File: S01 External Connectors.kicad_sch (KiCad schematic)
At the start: 43 parts, among them J1 1053101204, J2 1053101114, J3 10144517-043802LF, J4 1053102204, J5 1053091102, J6 1053091102, M1 78614150960, M2 78614150960, M3 78614150960, M4 78614150960, M5 78614150960, M6 78614150960

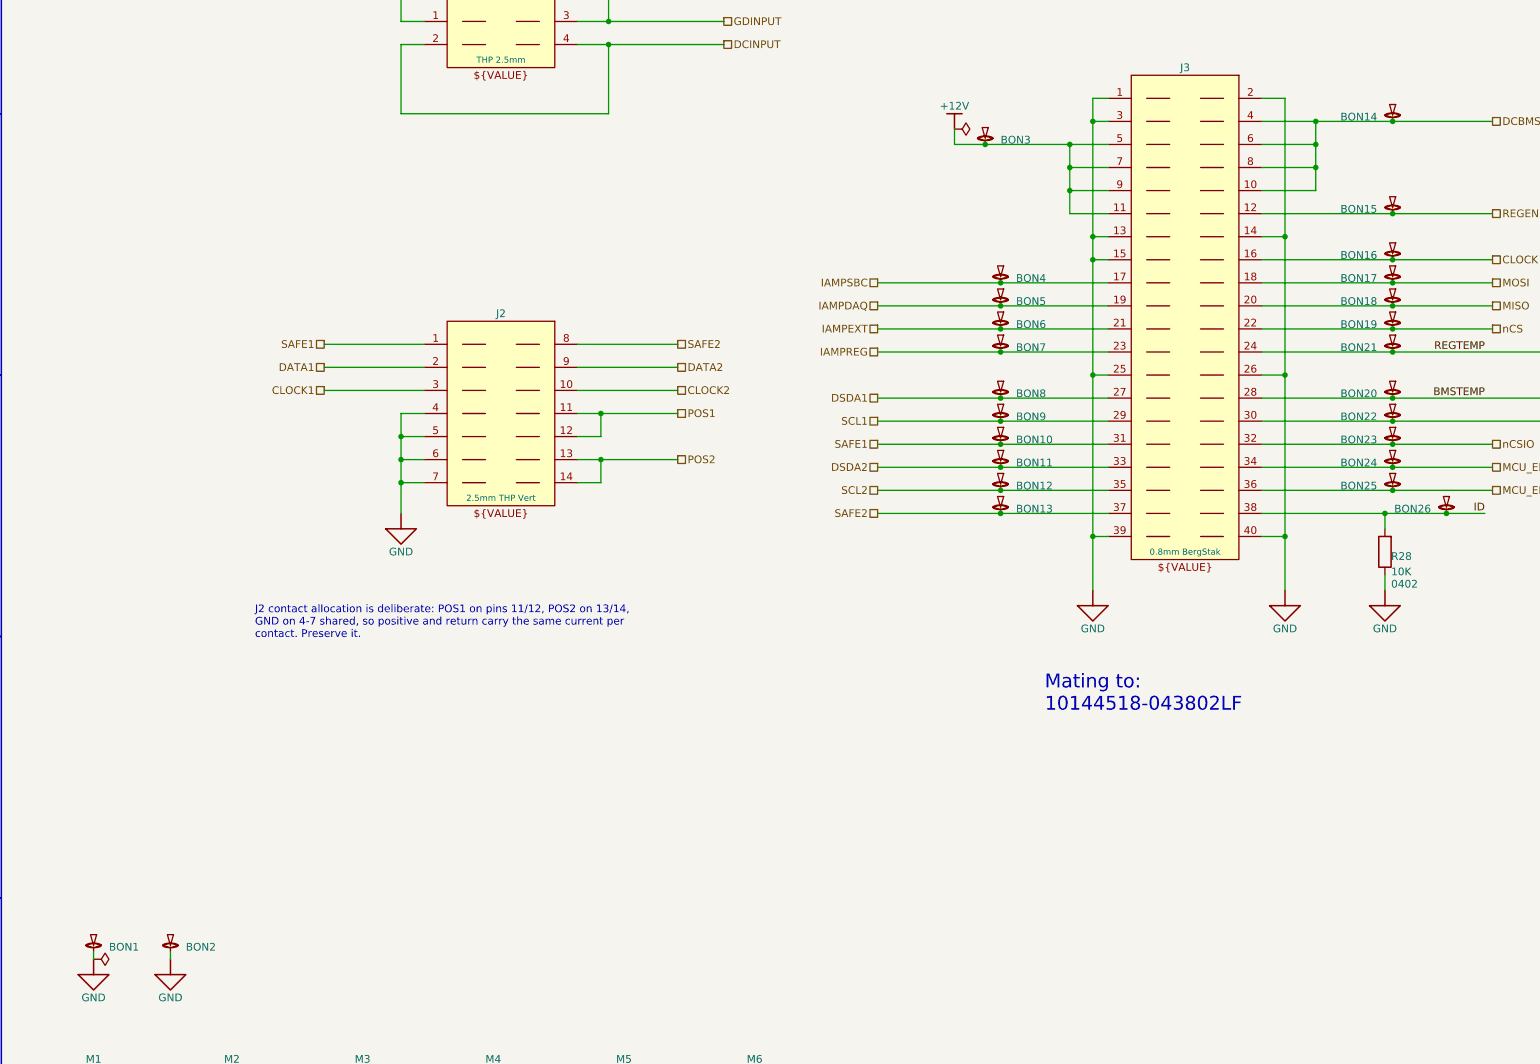
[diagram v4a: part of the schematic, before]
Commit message: New PG-TDSON-8-33 footprint for Q16/Q17/Q19; set SMD/THT types; BON pads to TP
- Q16/Q17/Q19 move to Infineon_PG-TDSON-8-33_5.48x5.15mm_P1.27mm, built from
  the IAUCN04S7L019 datasheet land pattern: centred copper, separate stencil
  apertures (2x2 windows, ~58% on the exposed pad). Pad numbering matches the
  existing symbol (source bar = 1, exposed pad = 8).
- Set the footprint type on 42 untyped imported parts (37 SMD, J1/J2/J4/J5/J6
  through-hole), on the board and in the project library, so they reach the
  SMD position file.
- Rename pogo test pads BON1-26 to TP1-26, exclude them from BOM and position
  files, and point the 0.3 mm pad-to-pad DRC rule at TP*.

DRC: 0 errors, 0 unconnected. ERC: 0 violations.

Co-Authored-By: Claude Opus 5.5 <noreply@anthropic.com>
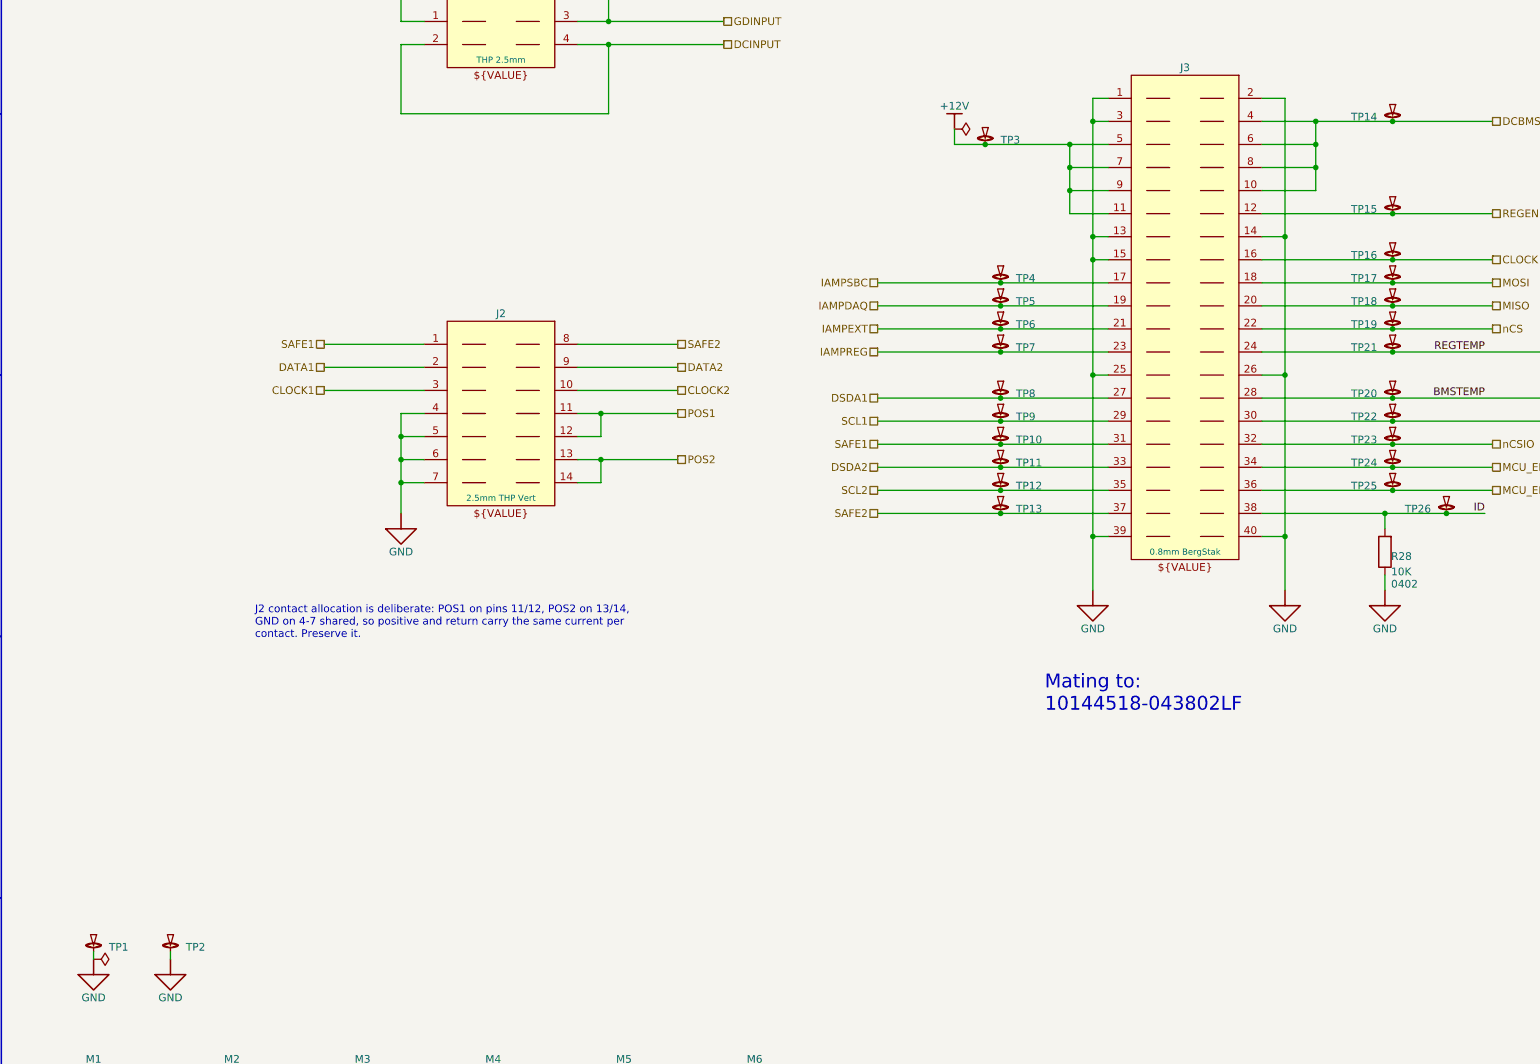
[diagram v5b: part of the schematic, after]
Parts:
- TP1: renamed from BON1; now left out of the parts list
- TP10: renamed from BON10; now left out of the parts list
- TP11: renamed from BON11; now left out of the parts list
- TP12: renamed from BON12; now left out of the parts list
- TP13: renamed from BON13; now left out of the parts list
- TP14: renamed from BON14; now left out of the parts list
- TP15: renamed from BON15; now left out of the parts list
- TP16: renamed from BON16; now left out of the parts list
- TP17: renamed from BON17; now left out of the parts list
- TP18: renamed from BON18; now left out of the parts list
- TP19: renamed from BON19; now left out of the parts list
- TP2: renamed from BON2; now left out of the parts list
- TP20: renamed from BON20; now left out of the parts list
- TP21: renamed from BON21; now left out of the parts list
- TP22: renamed from BON22; now left out of the parts list
- TP23: renamed from BON23; now left out of the parts list
- TP24: renamed from BON24; now left out of the parts list
- TP25: renamed from BON25; now left out of the parts list
- TP26: renamed from BON26; now left out of the parts list
- TP3: renamed from BON3; now left out of the parts list
- TP4: renamed from BON4; now left out of the parts list
- TP5: renamed from BON5; now left out of the parts list
- TP6: renamed from BON6; now left out of the parts list
- TP7: renamed from BON7; now left out of the parts list
- TP8: renamed from BON8; now left out of the parts list
- TP9: renamed from BON9; now left out of the parts list

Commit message: Spacers to SMD on one footprint; drop Altium no-paste pad margins
- M1-M6 (Wurth 78614150960, tape-fed, reflowed) are set to SMD so they reach
  the SMD position file. M1 moves to the same footprint as M2-M6; the
  duplicate lowercase spacer footprint is removed.
- Remove the Altium "no paste" solder_paste_margin (and the paste layer it
  blanked) from the spacer, U1/U5 exposed-pad and TP test-pad pads, on the
  board and in the library. Clears all 34 padstack DRC warnings; copper,
  mask and paste Gerbers are unchanged apart from draw order.

DRC: 0 errors, 0 unconnected.

Co-Authored-By: Claude Opus 5.5 <noreply@anthropic.com>
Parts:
- M1: footprint EVO2513-0_5_0-import-fps:Mech Spacer Wurth 78614150960 Through M3 -> EVO2513-0_5_0-import-fps:MECH SPACER WURTH 78614150960 THROUGH M3
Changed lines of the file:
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@@
 			)
 		)
-		(property "Footprint" "EVO2513-0_5_0-import-fps:Mech Spacer Wurth 78614150960 Through M3"
+		(property "Footprint" "EVO2513-0_5_0-import-fps:MECH SPACER WURTH 78614150960 THROUGH M3"
 			(at 17.78 267.97 0)
 			(hide yes)

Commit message: Fiducials: placement file, no paste, 3 mm mask opening with copper keepout
- Fiducial1/2 are SMD and in the position file, excluded from the BOM
  (schematic, symbol library and footprints agree).
- Remove the paste layer from the fiducial pad; the stencil was printing a
  1.27 mm paste dot on each fiducial.
- Fiducial-50 gets a 0.865 mm mask margin (3.0 mm opening on the 1.27 mm pad)
  and a 3.2 mm F.Cu keepout (no pour, tracks or vias) so no other copper shows
  in the opening.
- Remove two GND stitching vias inside Fiducial1's clear area; zones refilled.

DRC: 0 errors, 0 unconnected. ERC: 0 violations.

Co-Authored-By: Claude Opus 5.5 <noreply@anthropic.com>
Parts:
- Fiducial1, Fiducial2: now left out of the parts list
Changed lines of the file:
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@@
 		(body_style 1)
 		(exclude_from_sim no)
-		(in_bom yes)
+		(in_bom no)
 		(on_board yes)
 		(in_pos_files yes)
@@
 		(body_style 1)
 		(exclude_from_sim no)
-		(in_bom yes)
+		(in_bom no)
 		(on_board yes)
 		(in_pos_files yes)

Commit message: Fix J3 and Q16/Q17/Q19 part numbers; stackup to the fab drawing
- J3 MANUFACTURER_PN 10144517-042802LF -> 10144517-043802LF, matching
  its value and footprint. The wrong number came from the Altium part
  list.
- Q16/Q19 IAUCN04S7L019ATMA1 and Q17 IAUCN04S7L028ATMA1 in place of
  the package name PG-TDSON-8-33; manufacturer "Infenion" -> Infineon.
- PCB stackup set to the Altium fab drawing: 0.25 mm cores, 2116
  prepregs (doubled between In2/In3 and In4/In5), 0.035 mm outer and
  0.030 mm inner copper, 0.013 mm mask, ENIG. 1.59 mm laminate,
  1.598 mm finished.
- Stackup drawing: second layer label "L1" -> "L2".

Co-Authored-By: Claude Opus 5.5 <noreply@anthropic.com>
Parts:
- J3: MANUFACTURER_PN 10144517-042802LF -> 10144517-043802LF
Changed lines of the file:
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@@
 			)
 		)
-		(property "MANUFACTURER_PN" "10144517-042802LF"
+		(property "MANUFACTURER_PN" "10144517-043802LF"
 			(at 184.912 93.98 0)
 			(hide yes)
